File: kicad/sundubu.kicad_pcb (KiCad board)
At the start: 2 copper layers, 100 x 92 mm, 45 parts, among them J1 AudioJack4, J2 AudioJack4, SW1 SW_Push, SW10 SW_Push, SW11 SW_Push, SW12 SW_Push, SW13 SW_Push, SW14 SW_Push, SW15 SW_Push, SW16 SW_Push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

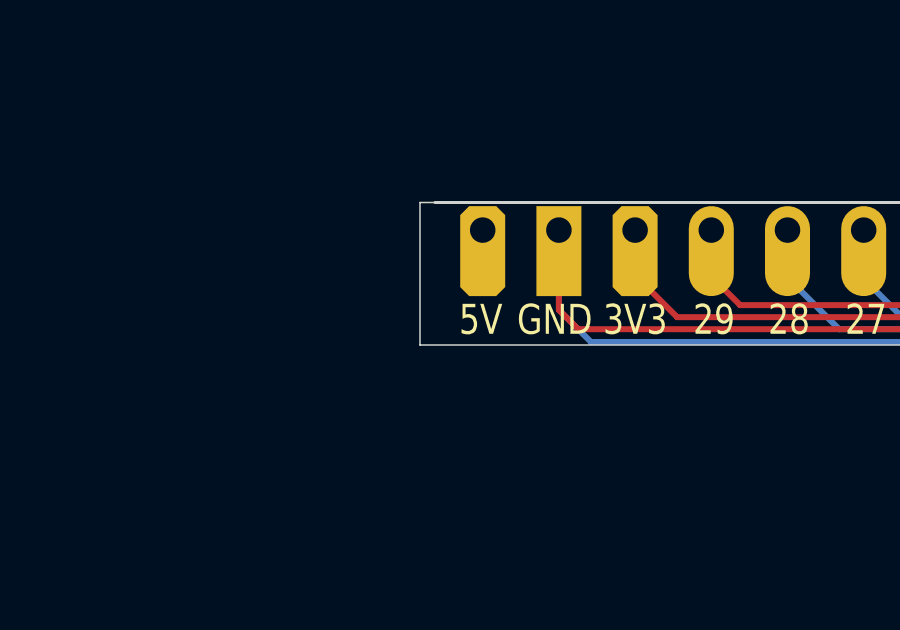
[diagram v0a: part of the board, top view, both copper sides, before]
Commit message: edit gerber ground via
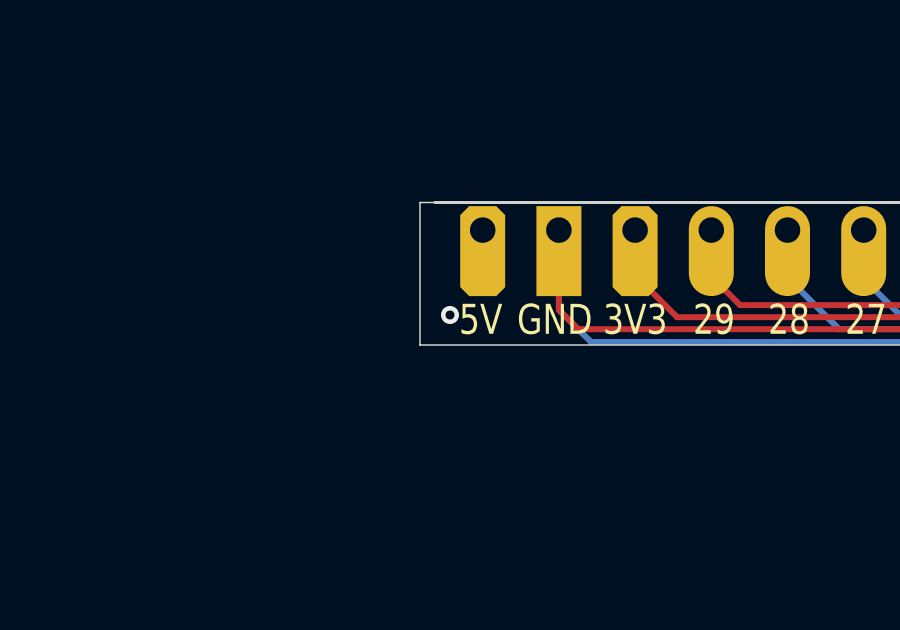
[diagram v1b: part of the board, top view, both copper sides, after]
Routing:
- net GND: vias 40 -> 41
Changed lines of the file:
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@@
+	)
+	(via
+		(at 56.5 137.5)
+		(size 0.6)
+		(drill 0.3)
+		(layers "F.Cu" "B.Cu")
+		(net 12)
 	)
 	(via
